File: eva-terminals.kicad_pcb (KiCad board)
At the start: 2 copper layers, 64 x 54 mm, 24 parts, among them J1 RIBBON, J4 EXTRUDER, J5 HEATER, J6 SPI, J7 AUX, U1 LD39015M33R, U2 ADXL345

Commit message: wip dual ribbon
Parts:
- removed C7: 1U, Capacitor_SMD:C_0805_2012Metric
- removed the J1 at (100.0, 101.9)
- removed the J4 at (101.5, 74.5)
- removed JP5: SolderJumper_2_Open, Jumper:SolderJumper-2_P1.3mm_Open_RoundedPad1.0x1.5mm
- added C8: 1U, Capacitor_SMD:C_0805_2012Metric, F.Cu at (92.0, 72.5)
- added D1: WS2812B, LED_SMD:LED_WS2812B_PLCC4_5.0x5.0mm_P3.2mm, B.Cu at (91.8, 72.5)
- added J2: 691403900006B, Eagle_WR-TBL Spring Clamp (rev21a):691403900006B, B.Cu at (126.8, 104.0)
- added J3: Conn_01x04_dualpin, Eagle_WR-TBL Spring Clamp (rev21a):691402910004B, F.Cu at (105.3, 74.8)
- added J6: Conn_02x10_Odd_Even, Eagle_WR-MM (rev20b):690367292076, F.Cu at (106.0, 100.0)
- added JP7: SolderJumper_2_Open, Jumper:SolderJumper-2_P1.3mm_Open_RoundedPad1.0x1.5mm, F.Cu at (114.3, 110.9)
- added JP8: SolderJumper_2_Open, Jumper:SolderJumper-2_P1.3mm_Open_RoundedPad1.0x1.5mm, F.Cu at (119.0, 91.3)
- added TH1: PT1000, Resistor_SMD:R_1206_3216Metric, F.Cu at (91.8, 60.5)
- added U3: 74AUP1G32, Package_TO_SOT_SMD:SOT-553, F.Cu at (95.5, 118.0)
- J7: value AUX -> Conn_02x10_Odd_Even; footprint Eagle_WR-TBL Spring Clamp (rev21a):691403900004B -> Eagle_WR-MM (rev20b):690367292076; moved to F.Cu
- moved J7 33.5 mm to (94.0, 100.0), turned to 90 degrees
- moved C1 26.5 mm to (110.5, 114.5), turned to 0 degrees
- moved U1 20.5 mm to (109.5, 118.0), turned to 90 degrees
- moved C2 20.4 mm to (106.5, 118.0)
- moved R1 17.7 mm to (87.5, 91.5)
- moved C3 15.8 mm to (104.5, 118.0), turned to -90 degrees
- moved FB1 14.3 mm to (100.0, 114.5), turned to 180 degrees
- moved C4 13.8 mm to (121.5, 91.5), turned to -90 degrees
- moved C5 13.1 mm to (121.5, 80.8), turned to 90 degrees
- moved C6 13.0 mm to (78.5, 82.0), turned to 90 degrees
- moved JP1 12.4 mm to (116.6, 91.3), turned to 90 degrees
- moved JP6 11.7 mm to (119.1, 110.8), turned to 90 degrees
- moved U2 9.04 mm to (100.0, 118.0)
- moved JP2 8.99 mm to (114.2, 91.3), turned to 90 degrees
- moved JP3 5.60 mm to (111.8, 91.3), turned to 90 degrees
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- renumbered LEFT1 to J1, RIGHT1 to J4, J6 to J8
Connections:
- net SENSOR_M renamed GNDREF
- net SENSOR_P renamed HOTEND_TEMP
- C5 pad 2: +12V -> TOOL_FAN_PWR
- C6 pad 2: +12V -> PART_FAN_PWR
- J1 pad 1: +12V -> TOOL_FAN_PWR
- J1 pad 3: TOOL_FAN_TACH -> TOOL_FAN_TACH/PWM
- J1 pad A1: +12V -> TOOL_FAN_PWR
- J1 pad A3: TOOL_FAN_TACH -> TOOL_FAN_TACH/PWM
- J4 pad 6: +12V -> PART_FAN_PWR
- J4 pad A6: +12V -> PART_FAN_PWR
- J7 pad 1: AUX1 -> PART_FAN_PWR
- J7 pad 2: AUX2 -> PART_FAN_PWR
- J7 pad 3: AUX_PWR -> GND
- J8 pad 2: +5V -> CHAMBER_TEMP
- J8 pad A2: +5V -> CHAMBER_TEMP
- JP1 pad 2: +12V -> PART_FAN_PWR
- JP4 pad 1: AUX_PWR -> NEOPIXEL_IN
- JP4 pad 2: +12V -> /NEOPIXEL_RIBBON
- JP6 pad 1: AUX_PWR -> /NEOPIXEL_RIBBON
- JP6 pad 2: +3V3 -> /NEOPIXEL_TERMINAL
- U2 pad 13: SDA -> Net-(U2-Pad13)
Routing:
- net TOOL_FAN_TACH/PWM: track 0.00 -> 39.4 mm, vias 0 -> 1
- net TOOL_FAN_TACH: track 33.9 -> 0.00 mm
- net HOTEND_TEMP: track 33.7 -> 0.00 mm
- net PART_FAN_PWR: track 0.00 -> 31.5 mm
- net PROBE: track 35.0 -> 5.08 mm
- net GNDREF: track 28.6 -> 0.00 mm
- net /NEOPIXEL_RIBBON: track 0.00 -> 26.3 mm, vias 0 -> 1
- net SDO: track 31.1 -> 5.08 mm
- net TOOL_FAN_GND: track 29.9 -> 4.15 mm
- net CS: track 27.1 -> 5.08 mm
- net /NEOPIXEL_TERMINAL: track 0.00 -> 22.0 mm
- net SDI: track 25.3 -> 5.08 mm
- net SCLK: track 28.6 -> 11.6 mm
- net NEOPIXEL_IN: track 0.00 -> 16.8 mm, vias 0 -> 1
- net GND: track 20.3 -> 5.08 mm
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- added copper zone on B.Cu, net GND
- added copper zone on F.Cu, net GND
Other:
- board size 64 x 54 mm -> 64 x 64 mm
- board text added: "AUX3"
- board text added: "BOARD"
- board text added: "CHAMBER"
- board text added: "DNP HOTEND SIDE"
- board text added: "FAN+"
- board text added: "FAN-"
- board text added: "HOTEND"
- board text added: "LOCATION"
- board text added: "NEO"
- board text added: "PART"
- board text added: "PROBE VOLTAGE"
- board text added: "TOOL"
- board text removed: "APWR"

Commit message: finalized board layout rev 1
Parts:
- added REF**: OSHW-Logo_5.7x6mm_SilkScreen, Symbol:OSHW-Logo_5.7x6mm_SilkScreen, F.Cu at (84.6, 103.6)
- added REF**: OSHW-Logo_5.7x6mm_SilkScreen, Symbol:OSHW-Logo_5.7x6mm_SilkScreen, B.Cu at (106.9, 116.2)
- moved JP6 42.8 mm to (90.4, 79.0)
- moved JP4 42.4 mm to (84.1, 79.1)
- moved JP7 42.1 mm to (86.7, 79.1), turned to 90 degrees
- moved C1 15.7 mm to (94.8, 115.7), turned to -90 degrees
- moved U1 11.8 mm to (97.8, 116.2), turned to -90 degrees
- moved FB1 10.1 mm to (109.5, 118.0), turned to 90 degrees
- moved C2 5.24 mm to (101.3, 118.7), turned to 0 degrees
- moved U2 4.45 mm to (103.8, 115.7), turned to 90 degrees
- moved C4 3.71 mm to (120.6, 95.1)
- moved J6 2.00 mm to (106.0, 98.0)
- moved J7 2.00 mm to (94.0, 98.0)
- moved C3 1.92 mm to (106.3, 118.7), turned to 180 degrees
- moved R1 1.84 mm to (88.8, 90.2)
- moved JP8 1.70 mm to (120.7, 91.2)
- moved JP1 1.30 mm to (117.9, 91.2)
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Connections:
- J6 pad 10: /NEOPIXEL_RIBBON -> +5V
- J6 pad 11: HOTEND_TEMP -> +5V
- J6 pad 12: CHAMBER_TEMP -> GND
- J6 pad 13: SDO -> GND
- J6 pad 14: PROBE -> CS
- J6 pad 16: CS -> SDO
- J6 pad 17: AUX1 -> SDI
- J6 pad 18: SDI -> AUX1
- J6 pad 5: GND -> PROBE
- J6 pad 6: +5V -> /NEOPIXEL_RIBBON
- J6 pad 7: GND -> HOTEND_TEMP
- J6 pad 8: +5V -> GNDREF
- J6 pad 9: GNDREF -> CHAMBER_TEMP
- J7 pad 5: TOOL_FAN_TACH/PWM -> PART_FAN_PWM
- J7 pad 6: PART_FAN_PWM -> PART_FAN_TACH
- J7 pad 8: PART_FAN_TACH -> TOOL_FAN_PWR
- J7 pad 9: TOOL_FAN_PWR -> TOOL_FAN_TACH/PWM
- J8 pad 1: GND -> SDI
- J8 pad 2: CHAMBER_TEMP -> SDO
- J8 pad 4: SDI -> CS
- J8 pad 5: SDO -> CHAMBER_TEMP
- J8 pad 6: CS -> GND
- J8 pad A1: GND -> SDI
- J8 pad A2: CHAMBER_TEMP -> SDO
- J8 pad A4: SDI -> CS
- J8 pad A5: SDO -> CHAMBER_TEMP
- J8 pad A6: CS -> GND
- U2 pad 14: SCL -> SCLK
- U3 pad 2: SDA -> SDI
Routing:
- net +5V: track 5.08 -> 94.3 mm, vias 0 -> 4
- net GNDREF: track 0.00 -> 74.0 mm, vias 0 -> 3
- net TOOL_FAN_PWR: track 0.00 -> 65.5 mm, vias 0 -> 3
- net CHAMBER_TEMP: track 5.08 -> 59.2 mm, vias 0 -> 2
- net +3V3: track 0.00 -> 49.9 mm, vias 0 -> 2
- net HOTEND_TEMP: track 0.00 -> 42.6 mm, vias 0 -> 1
- net CS: track 5.08 -> 45.3 mm, vias 0 -> 3
- net TOOL_FAN_GND: track 4.15 -> 43.9 mm, vias 0 -> 1
- net /NEOPIXEL_TERMINAL: track 22.0 -> 56.6 mm, vias 0 -> 1
- net SDI: track 5.08 -> 35.1 mm, vias 0 -> 2
- net PART_FAN_PWR: track 31.5 -> 54.8 mm, vias 0 -> 2
- net AUX1: track 5.08 -> 27.8 mm
- net SDO: track 5.08 -> 26.5 mm
- net AUX3: track 5.08 -> 25.7 mm
- net GND: track 5.08 -> 23.1 mm, vias 0 -> 7
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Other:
- board text added: "Nema Toolboard Elco Jacobs"
- board text added: "Nema Toolboard by Elco Jacobs"
- board text removed: "12V"
- board text removed: "AUX"

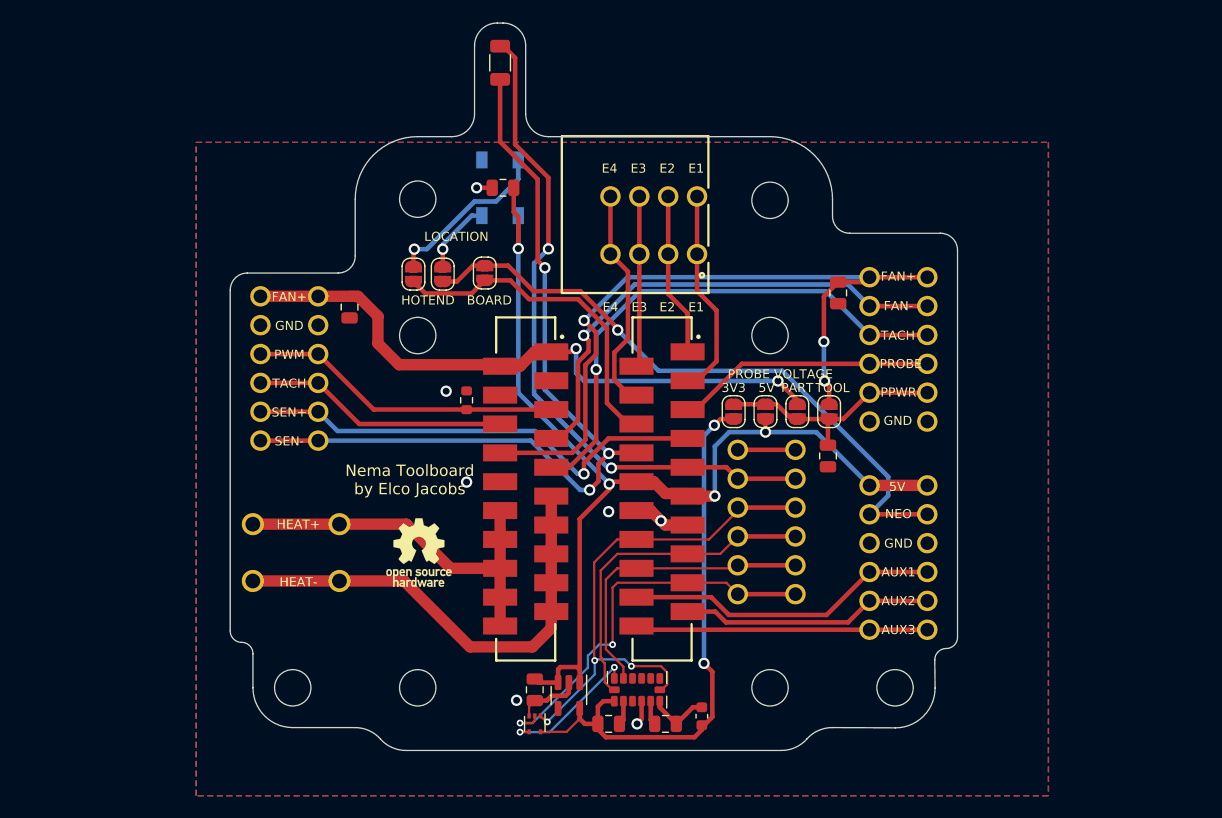
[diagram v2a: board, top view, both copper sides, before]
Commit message: more clearance for LGX bracket
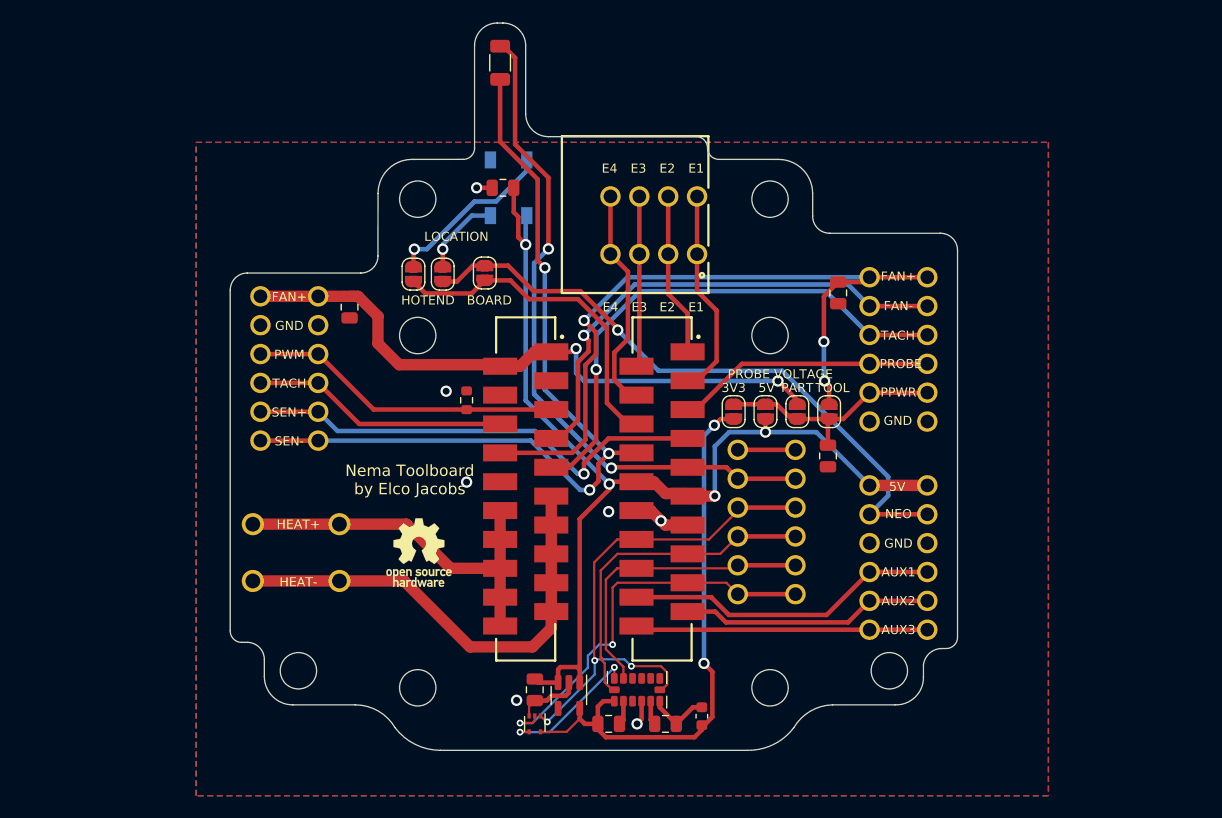
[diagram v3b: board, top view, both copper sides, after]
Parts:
- moved D1 0.75 mm to (92.5, 71.5)
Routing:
- net NEOPIXEL_OUT: track 6.46 -> 7.21 mm
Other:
- outline, holes or cut-outs redrawn

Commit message: jst-xh for stepper
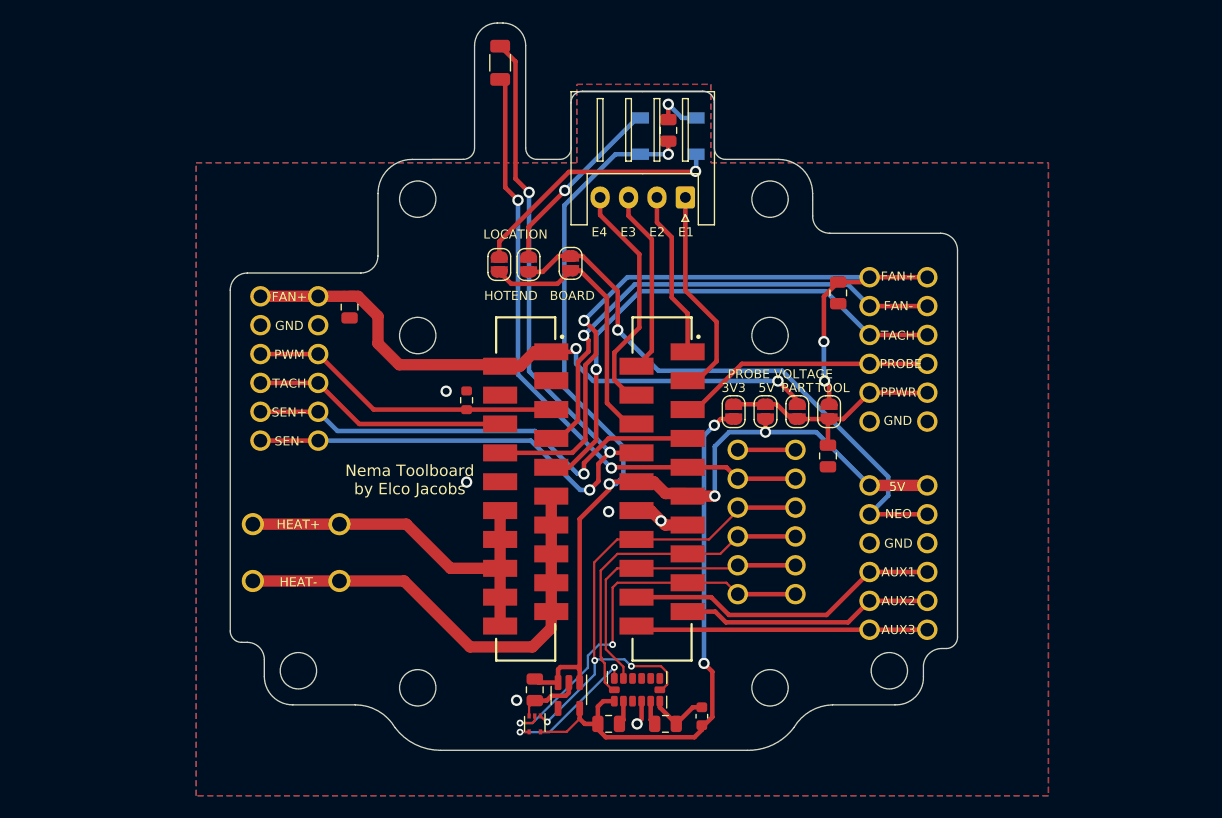
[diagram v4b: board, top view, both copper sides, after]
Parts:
- removed REF** (x2): OSHW-Logo_5.7x6mm_SilkScreen, Symbol:OSHW-Logo_5.7x6mm_SilkScreen
- J3: value Conn_01x04_dualpin -> Conn_01x04; footprint Eagle_WR-TBL Spring Clamp (rev21a):691402910004B -> Connector_JST:JST_XH_S4B-XH-A_1x04_P2.50mm_Horizontal
- moved C8 15.4 mm to (106.5, 66.5), turned to 90 degrees
- moved D1 14.8 mm to (106.5, 67.0), turned to 0 degrees
- moved JP4 7.60 mm to (91.7, 78.2)
- moved JP6 7.60 mm to (98.0, 78.2)
- moved JP7 7.60 mm to (94.2, 78.2)
- moved J3 3.71 mm to (108.0, 72.3)
- turned TH1 to 90 degrees
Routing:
- net NEOPIXEL_OUT: track 7.21 -> 16.5 mm
- net +5V: track 94.1 -> 101.6 mm
- net NEOPIXEL_IN: track 15.3 -> 22.7 mm
- net /NEOPIXEL_RIBBON: track 29.6 -> 24.0 mm
- net /NEOPIXEL_TERMINAL: track 56.6 -> 51.3 mm
- net CHAMBER_TEMP: track 59.2 -> 55.2 mm
- net GNDREF: track 74.0 -> 77.1 mm
- net GND: track 23.1 -> 26.0 mm
- net EXTRUDER_4: track 19.8 -> 20.9 mm
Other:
- outline, holes or cut-outs redrawn

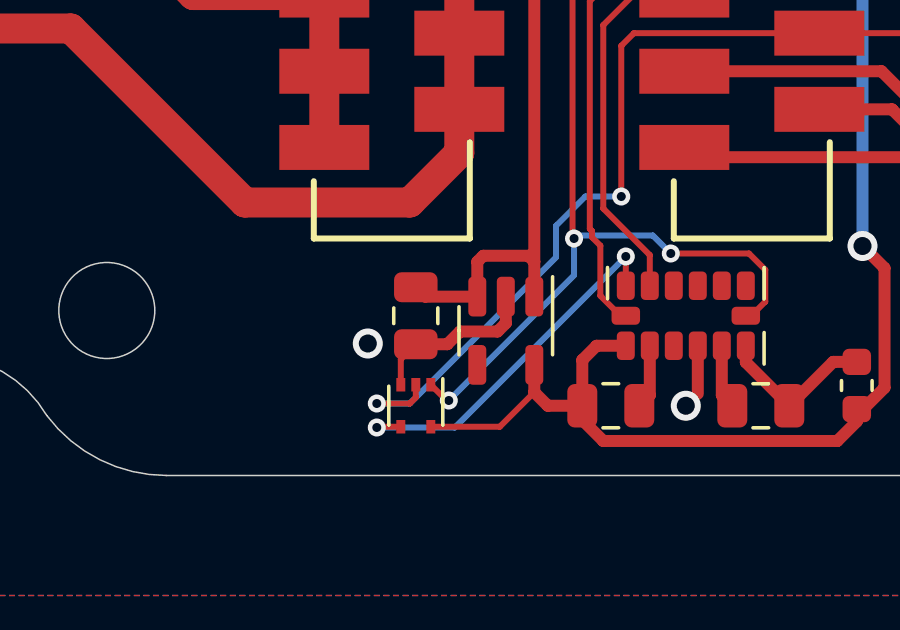
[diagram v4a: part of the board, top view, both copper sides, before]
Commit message: change footprint for OR gate
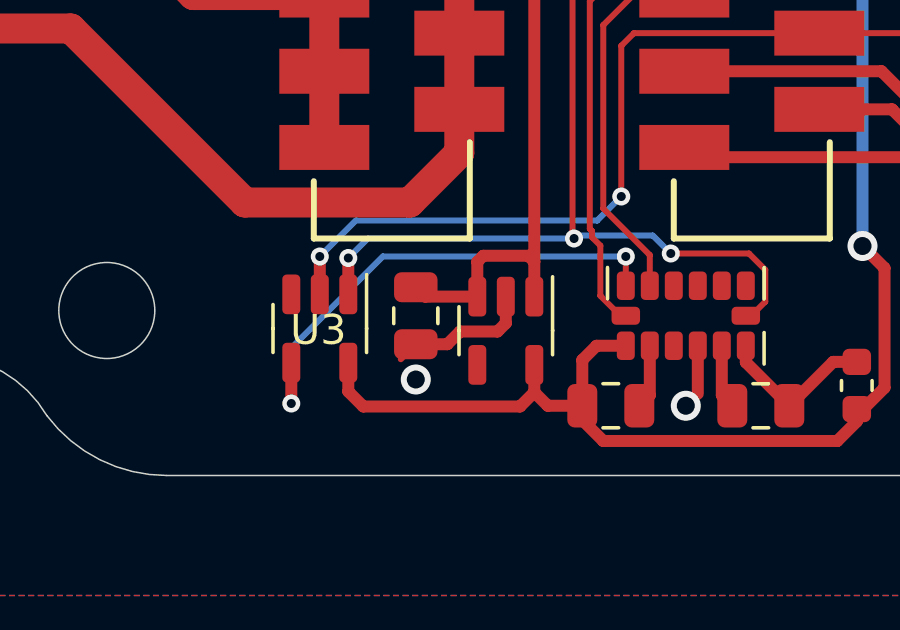
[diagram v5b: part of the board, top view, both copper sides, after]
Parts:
- R1: value 510R -> 470R
- U3: value 74AUP1G32 -> SN74LVC1G32DBVR‎; footprint Package_TO_SOT_SMD:SOT-553 -> Package_TO_SOT_SMD:SOT-23-5
- moved U3 4.11 mm to (91.6, 116.1)
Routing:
- net Net-(U2-Pad13): track 12.4 -> 16.6 mm
- net +3V3: track 49.9 -> 53.5 mm
- net SDI: track 35.1 -> 33.8 mm
- net CS: track 45.3 -> 46.3 mm
- net GND: track 26.0 -> 25.2 mm

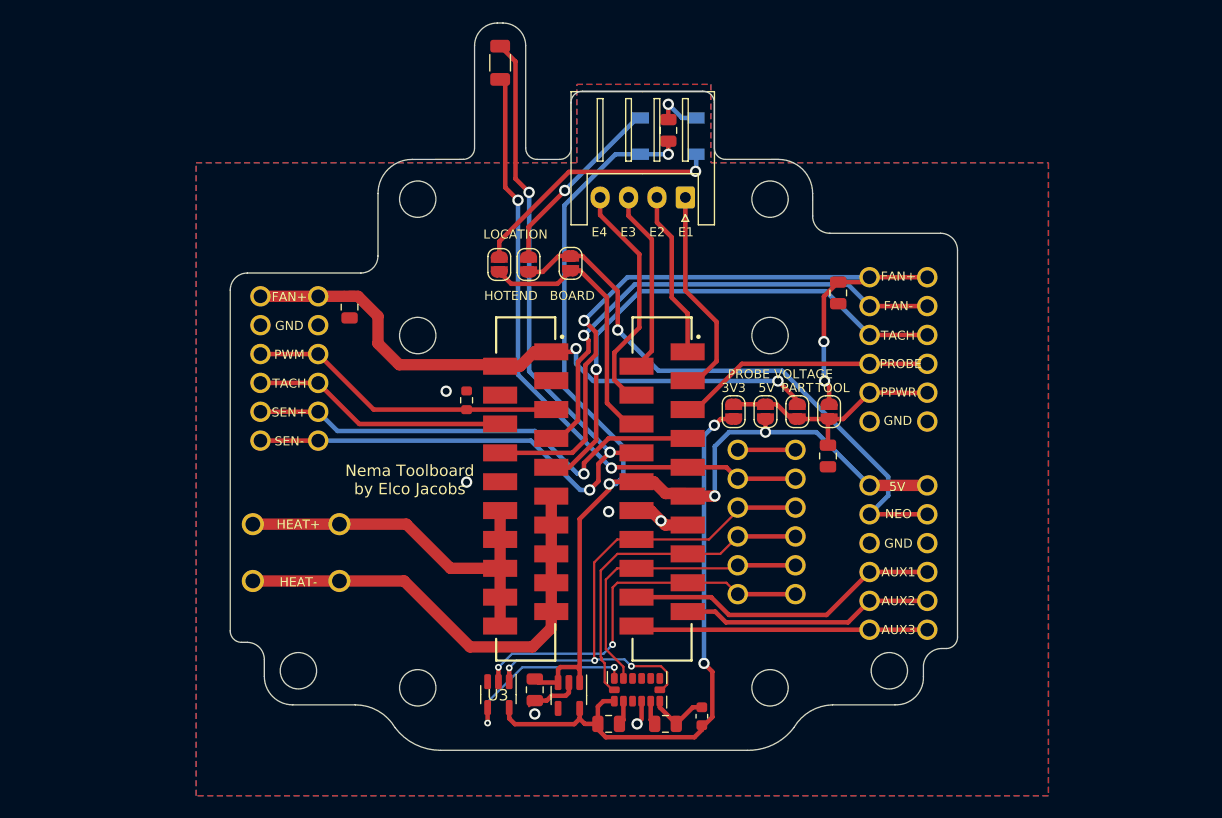
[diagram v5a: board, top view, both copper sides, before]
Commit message: add heater voltage to selection for probe
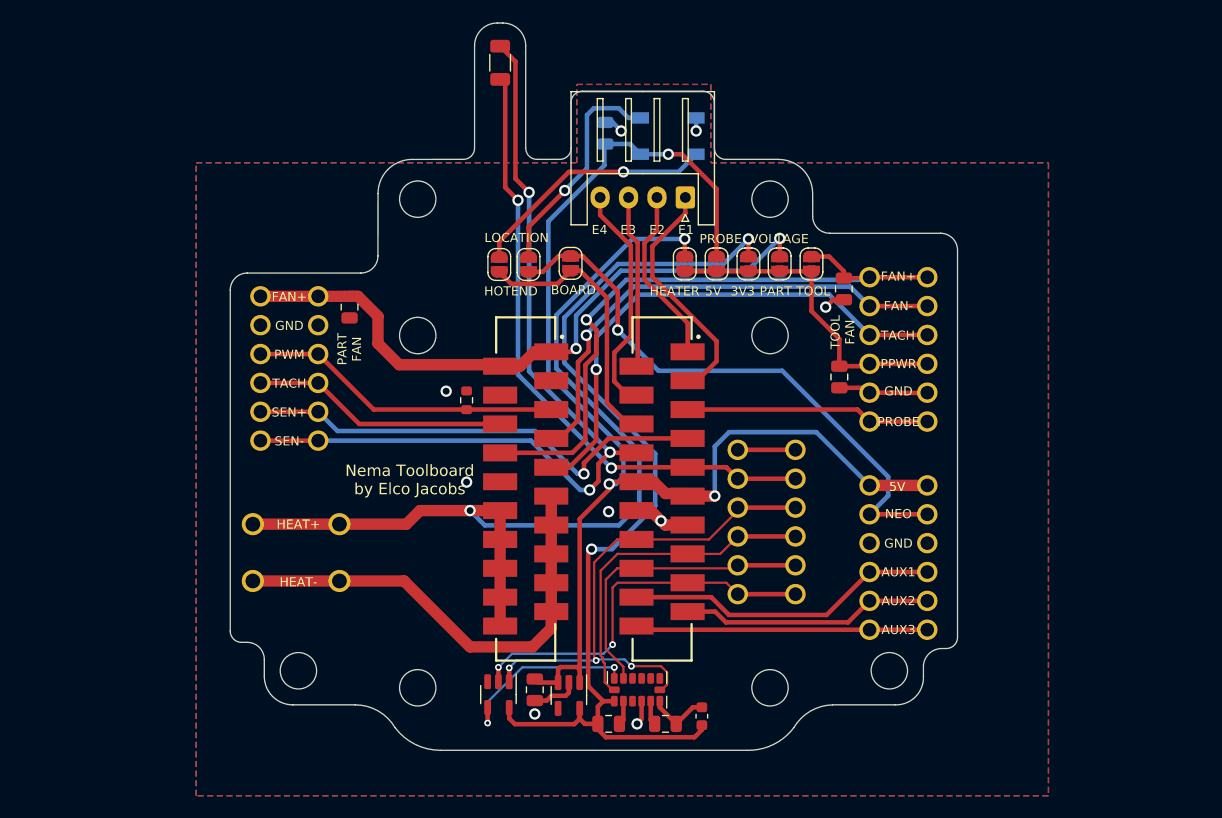
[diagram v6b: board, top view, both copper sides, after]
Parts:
- added JP5: SolderJumper_2_Open, Jumper:SolderJumper-2_P1.3mm_Open_RoundedPad1.0x1.5mm, F.Cu at (108.0, 78.2)
- C8: moved to B.Cu
- moved JP2 13.7 mm to (110.8, 78.2), turned to 90 degrees
- moved JP1 13.1 mm to (116.3, 78.2)
- moved JP8 13.1 mm to (119.2, 78.2)
- moved JP3 13.1 mm to (113.6, 78.2), turned to 90 degrees
- moved C4 7.02 mm to (121.6, 88.2)
- moved C8 5.56 mm to (101.0, 66.7)
- moved C5 0.61 mm to (122.0, 80.4)
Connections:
- J1 pad 4: PROBE -> PROBE_PWR
- J1 pad 5: PROBE_PWR -> GND
- J1 pad 6: GND -> PROBE
- J1 pad A4: PROBE -> PROBE_PWR
- J1 pad A5: PROBE_PWR -> GND
- J1 pad A6: GND -> PROBE
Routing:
- net HEATER_PWR: track 33.5 -> 83.9 mm, vias 0 -> 2
- net +3V3: track 53.5 -> 85.8 mm
- net +5V: track 101.6 -> 113.7 mm, vias 4 -> 3
- net TOOL_FAN_PWR: track 65.5 -> 57.1 mm, vias 3 -> 1
- net GND: track 25.2 -> 32.9 mm, vias 7 -> 9
- net PROBE_PWR: track 21.4 -> 28.3 mm
- net NEOPIXEL_OUT: track 16.5 -> 19.9 mm
- net PART_FAN_PWR: track 54.4 -> 57.1 mm
- net EXTRUDER_1: track 18.8 -> 21.2 mm
- net PROBE: track 22.8 -> 21.5 mm
- net EXTRUDER_2: track 14.7 -> 15.6 mm
- net HOTEND_TEMP: track 42.6 -> 41.7 mm
- net NEOPIXEL_IN: track 22.7 -> 21.9 mm
- net EXTRUDER_4: track 20.9 -> 20.4 mm
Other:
- board text added: "HEATER"
- board text added: "PART FAN"
- board text added: "TOOL FAN"
